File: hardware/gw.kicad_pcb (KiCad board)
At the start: 4 copper layers, 51.2 x 33 mm, 19 parts, among them J1 USB_OTG, J2 Conn_01x04, U1 ESP-12F, U2 Ai-Thinker-Ra-02, U3 AMS1117-3.3

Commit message: Change placement of PU resistors
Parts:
- moved R4 3.44 mm to (122.9, 53.6)
- moved R7 3.43 mm to (123.0, 47.8)
- moved R3 3.42 mm to (119.5, 47.8)
- moved R5 3.42 mm to (119.5, 53.6)
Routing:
- net Net-(R4-Pad1): track 3.94 -> 8.09 mm
- net Net-(R5-Pad1): track 7.77 -> 3.87 mm
- net /SS: track 37.3 -> 34.8 mm
- net /BOOT: track 11.3 -> 9.18 mm
- net Net-(R3-Pad2): track 22.4 -> 21.5 mm

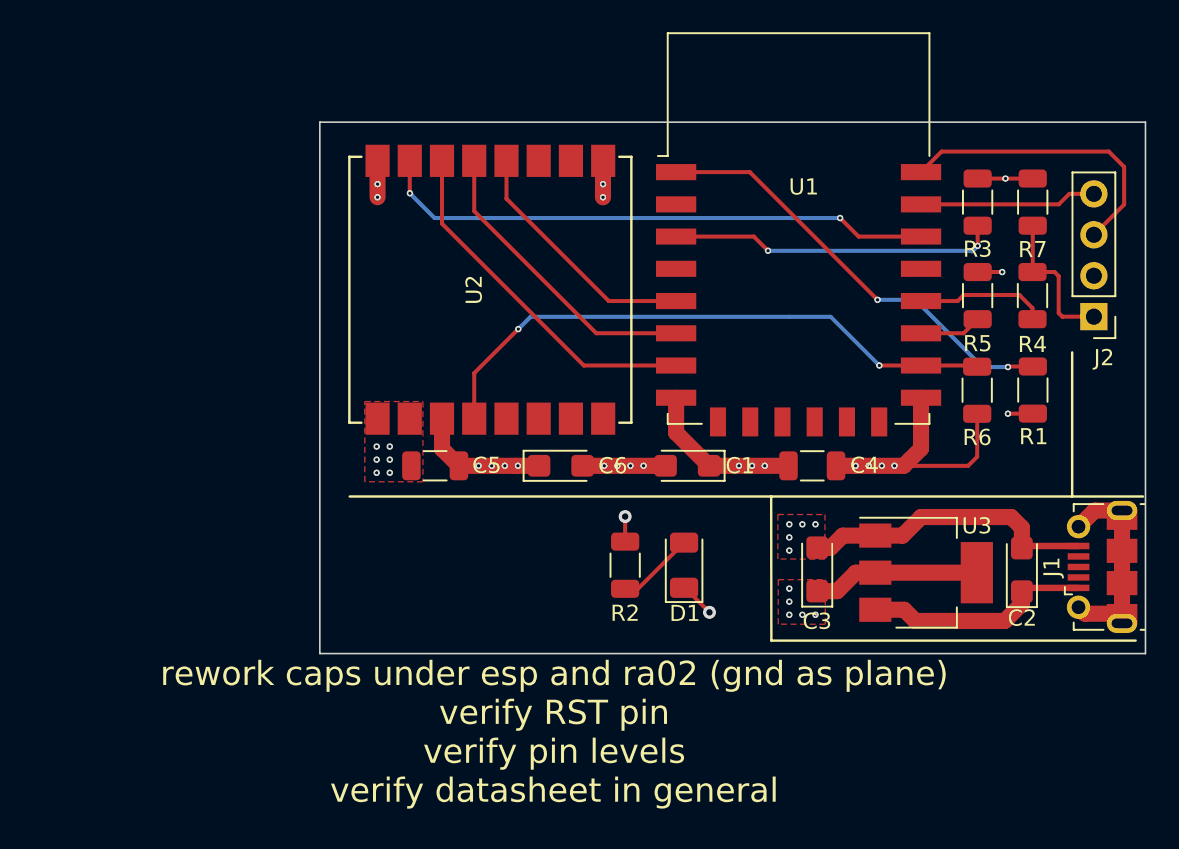
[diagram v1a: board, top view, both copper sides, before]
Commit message: Add leds, fix layout
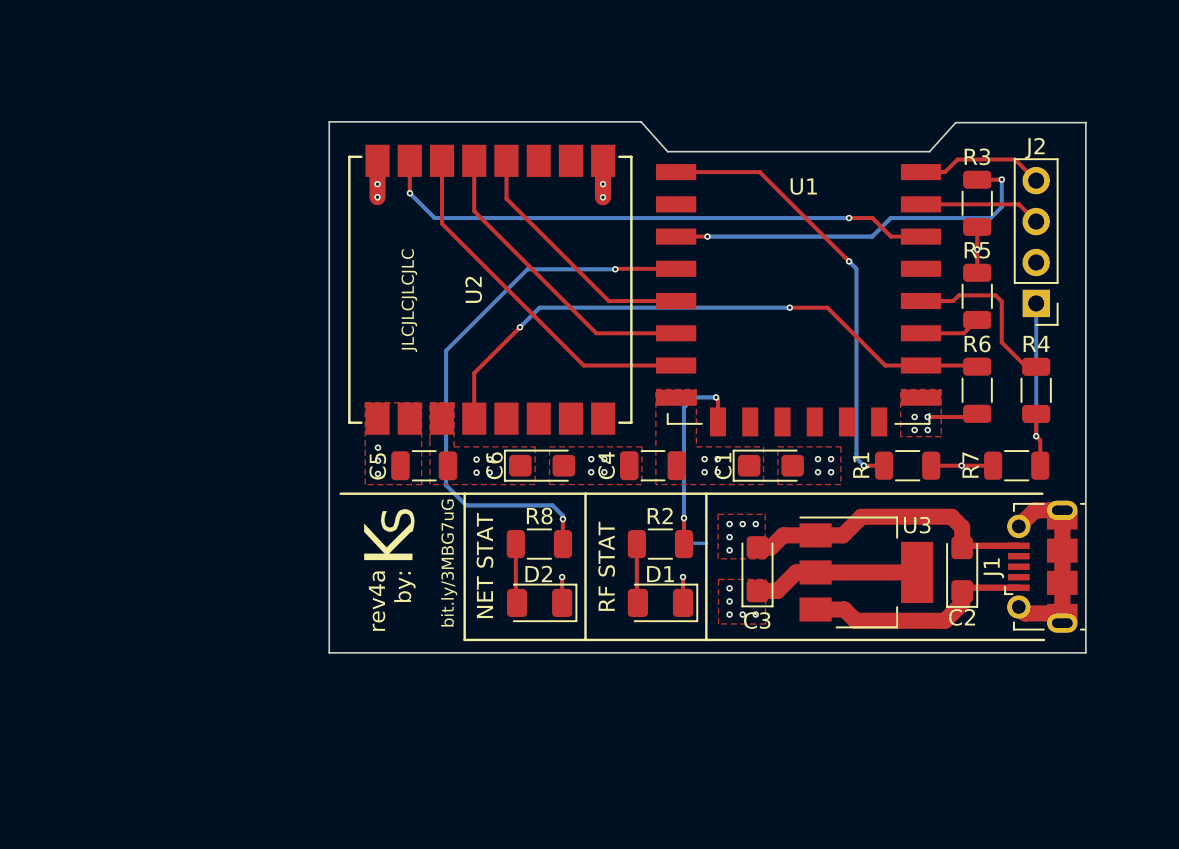
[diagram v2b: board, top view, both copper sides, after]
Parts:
- added D2: WIFI, LED_SMD:LED_1206_3216Metric, F.Cu at (92.3, 72.7)
- added R8: 220, Resistor_SMD:R_1206_3216Metric, F.Cu at (92.3, 69.0)
- C4: value 100nF -> 0.1µf
- C5: value 0.1uF -> 0.1µf
- D1: value CFG -> RF
- R2: value 220R -> 220
- moved R7 16.4 mm to (122.0, 64.2), turned to 180 degrees
- moved C4 9.88 mm to (99.4, 64.2), turned to 180 degrees
- moved R1 9.08 mm to (115.2, 64.2), turned to 180 degrees
- moved R4 5.88 mm to (123.2, 59.5), turned to -90 degrees
- moved C1 5.18 mm to (106.7, 64.2), turned to 0 degrees
- moved C2 3.71 mm to (118.6, 70.6)
- moved C3 3.71 mm to (105.9, 70.6)
- moved U3 3.71 mm to (112.6, 70.8)
- moved J1 3.71 mm to (123.6, 70.5)
- moved J2 3.67 mm to (123.2, 54.1)
- moved D1 2.76 mm to (99.8, 72.7), turned to 180 degrees
- moved R2 2.55 mm to (99.8, 69.0), turned to 0 degrees
- moved C6 1.16 mm to (92.5, 64.2)
- moved C5 0.68 mm to (85.2, 64.2)
- moved R3 0.08 mm to (119.5, 47.9), turned to 90 degrees
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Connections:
- J2 pad 3: /TXD -> /RXD
- J2 pad 4: /RXD -> /TXD
- R2 pad 2: Net-(R2-Pad2) -> Net-(U1-Pad9)
- U1 pad 19: /NSS -> unconnected-(U1-Pad19)
- U1 pad 20: /SS -> /NSS
- U1 pad 4: Net-(R2-Pad2) -> Net-(U1-Pad4)
- U1 pad 9: unconnected-(U1-Pad9) -> Net-(U1-Pad9)
- U2 pad 15: /SS -> /NSS
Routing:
- net /SS: track 34.8 -> 0.00 mm, vias 2 -> 0
- net /NSS: track 0.00 -> 34.8 mm, vias 0 -> 2
- net Net-(U1-Pad4): track 0.00 -> 34.5 mm, vias 0 -> 2
- net +3V3: track 35.2 -> 17.1 mm
- net GND: track 47.7 -> 29.7 mm, vias 24 -> 26
- net Net-(U1-Pad9): track 0.00 -> 12.3 mm, vias 0 -> 2
- net /TXD: track 18.5 -> 8.01 mm
- net Net-(D2-Pad2): track 0.00 -> 3.68 mm
- net /RXD: track 11.0 -> 7.59 mm
- net Net-(R3-Pad2): track 21.5 -> 24.2 mm
- net Net-(R4-Pad1): track 8.09 -> 10.6 mm
- net /BOOT: track 9.18 -> 11.6 mm, vias 0 -> 1
- net Net-(R2-Pad2): track 1.56 -> 0.00 mm, vias 1 -> 0
- net Net-(D1-Pad2): track 4.84 -> 3.68 mm
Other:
- board size 51.2 x 33 mm -> 47 x 32.9 mm
- board text added: "JLCJLCJLCJLC"
- board text added: "K"
- board text added: "NET STAT"
- board text added: "RF STAT"
- board text added: "S"
- board text added: "bit.ly/3MBG7uG"
- board text added: "rev4a by:"
- board text removed: "rework caps under esp and ra02 (gnd as plane) verify RST pin verify pin levels verify datasheet in general"

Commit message: Update schematics, almost fab ready
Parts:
- U1: footprint RF_Module:ESP-12E -> RF_Module:ESP-07
- moved U1 1.38 mm to (108.4, 50.9)
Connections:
- R2 pad 2: Net-(U1-Pad9) -> /RF_LED
- R4 pad 1: Net-(R4-Pad1) -> /WF_LED
- R5 pad 1: Net-(R5-Pad1) -> /DIO0
- R8 pad 2: Net-(U1-Pad4) -> /WF_LED
- U1 pad 10: unconnected-(U1-Pad10) -> /RESET
- U1 pad 11: unconnected-(U1-Pad11) -> /DIO0
- U1 pad 12: unconnected-(U1-Pad12) -> /WF_LED
- U1 pad 13: unconnected-(U1-Pad13) -> /DIO2
- U1 pad 14: unconnected-(U1-Pad14) -> /NSS
- U1 pad 15: GND -> /RXD
- U1 pad 16: /RESET -> /TXD
- U1 pad 4: Net-(U1-Pad4) -> /RF_LED
- U1 pad 9: Net-(U1-Pad9) -> GND
- U2 pad 5: unconnected-(U2-Pad5) -> /DIO0
- U2 pad 7: unconnected-(U2-Pad7) -> /DIO2
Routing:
- net /WF_LED: track 0.00 -> 59.5 mm, vias 0 -> 2
- net Net-(U1-Pad4): track 34.5 -> 0.00 mm, vias 2 -> 0
- net /DIO0: track 0.00 -> 33.1 mm, vias 0 -> 2
- net /DIO2: track 0.00 -> 29.0 mm, vias 0 -> 2
- net /RF_LED: track 0.00 -> 20.7 mm, vias 0 -> 2
- net Net-(U1-Pad9): track 12.3 -> 0.00 mm, vias 2 -> 0
- net Net-(R4-Pad1): track 10.6 -> 0.00 mm
- net Net-(R1-Pad2): track 27.3 -> 33.6 mm, vias 2 -> 0
- net Net-(R5-Pad1): track 3.83 -> 0.00 mm
- net /RESET: track 37.2 -> 36.2 mm
- net /NSS: track 34.8 -> 35.4 mm
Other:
- board text added: "bit.ly /3MBG7uG"
- board text added: "rev: m4a by:"
- board text removed: "bit.ly/3MBG7uG"
- board text removed: "rev4a by:"

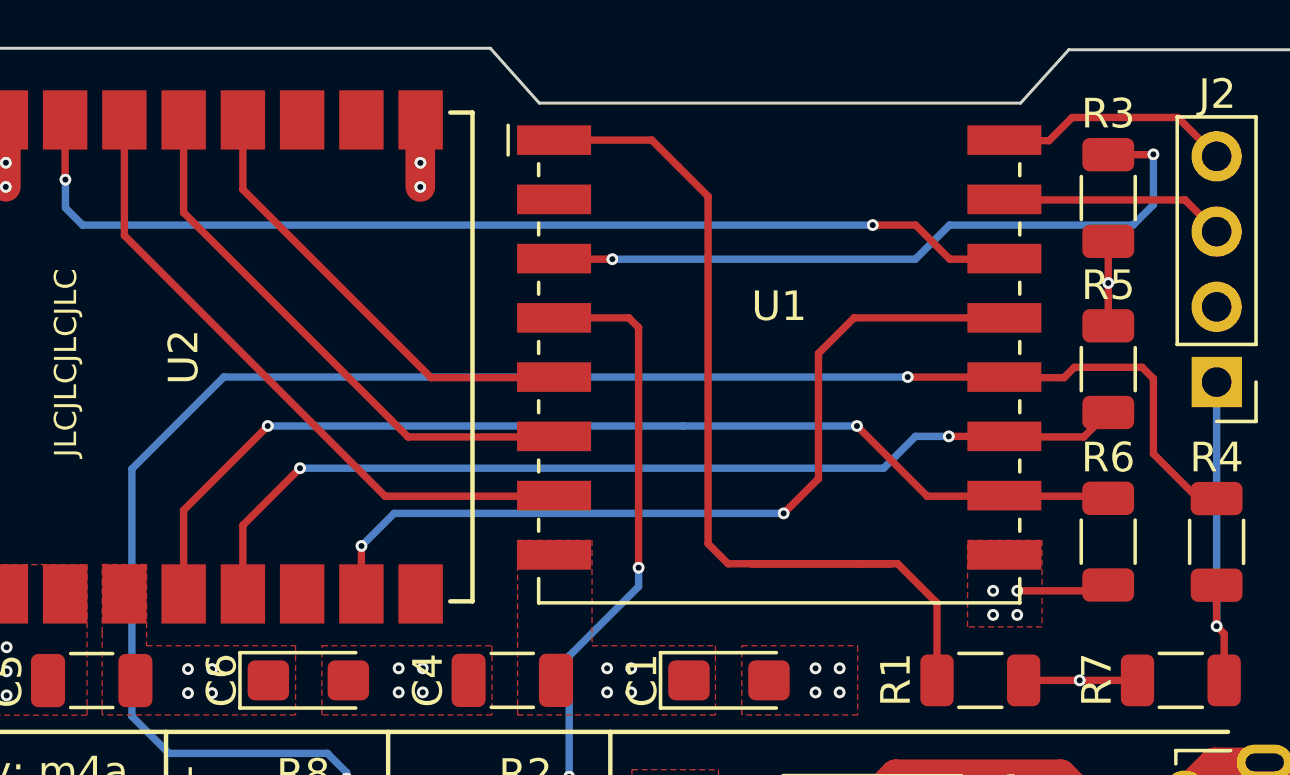
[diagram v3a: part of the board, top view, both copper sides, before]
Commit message: Add DIO1 pin support
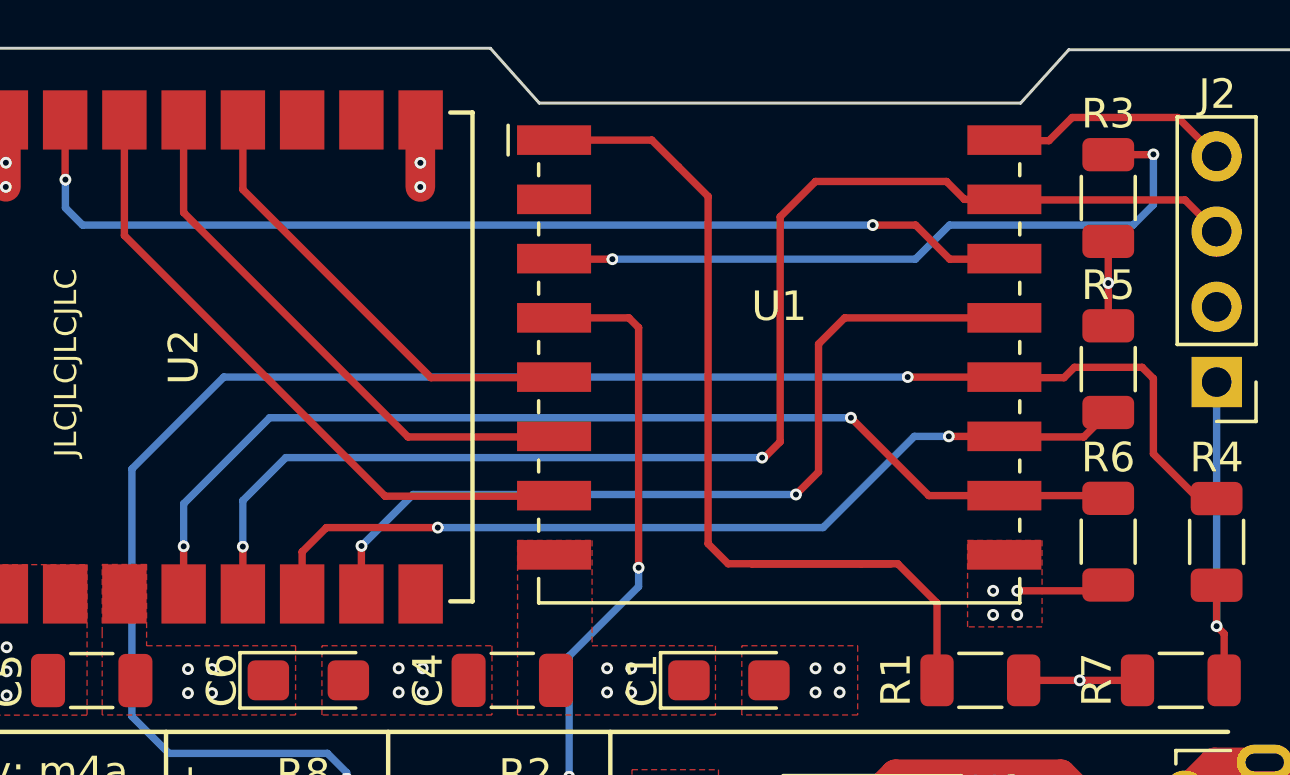
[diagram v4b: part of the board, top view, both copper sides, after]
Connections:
- net /NSS renamed /SS
- R5 pad 1: /DIO0 -> /DIO1
- U1 pad 11: /DIO0 -> /DIO1
- U2 pad 5: /DIO0 -> /RXD
- U2 pad 6: unconnected-(U2-Pad6) -> /DIO1
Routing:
- net /RXD: track 7.59 -> 45.6 mm, vias 0 -> 2
- net /DIO0: track 33.1 -> 0.00 mm, vias 2 -> 0
- net /DIO1: track 0.00 -> 30.6 mm, vias 0 -> 2
